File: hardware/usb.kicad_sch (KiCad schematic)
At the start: 16 parts, among them J4 USB_C_Receptacle_USB2.0_14P, J5 USB_C_Receptacle_USB2.0_14P, J6 USB_C_Receptacle_USB2.0_14P, U1 ECP5U_12_CABGA256, U10 TPD2EUSB30A, U6 FT231XQ, U8 TPD2EUSB30A, U9 TPD2EUSB30A

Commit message: Routed most of sdram
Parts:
- R15, R16, R17, R18, R19, R20: footprint Resistor_SMD:R_0603_1608Metric -> Resistor_SMD:R_0402_1005Metric
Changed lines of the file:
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@@
 			)
 		)
-		(property "Datasheet" ""
+		(property "Datasheet" "https://www.lcsc.com/datasheet/lcsc_datasheet_2411220131_Lattice-LFE5U-25F-6BG256C_C1521614.pdf"
 			(at 147.32 2.54 0)
 			(effects
@@
 			)
 		)
-		(property "Footprint" "Resistor_SMD:R_0603_1608Metric"
+		(property "Footprint" "Resistor_SMD:R_0402_1005Metric"
 			(at 54.61 155.702 90)
 			(effects
@@
 			)
 		)
-		(property "Footprint" "Resistor_SMD:R_0603_1608Metric"
+		(property "Footprint" "Resistor_SMD:R_0402_1005Metric"
 			(at 62.23 29.972 90)
 			(effects
@@
 			)
 		)
-		(property "Footprint" "Resistor_SMD:R_0603_1608Metric"
+		(property "Footprint" "Resistor_SMD:R_0402_1005Metric"
 			(at 54.61 156.718 90)
 			(effects
@@
 			)
 		)
-		(property "Footprint" "Resistor_SMD:R_0603_1608Metric"
+		(property "Footprint" "Resistor_SMD:R_0402_1005Metric"
 			(at 55.88 98.552 90)
 			(effects
@@
 			)
 		)
-		(property "Footprint" "Resistor_SMD:R_0603_1608Metric"
+		(property "Footprint" "Resistor_SMD:R_0402_1005Metric"
 			(at 55.88 99.568 90)
 			(effects
@@
 			)
 		)
-		(property "Footprint" "Resistor_SMD:R_0603_1608Metric"
+		(property "Footprint" "Resistor_SMD:R_0402_1005Metric"
 			(at 62.23 30.988 90)
 			(effects

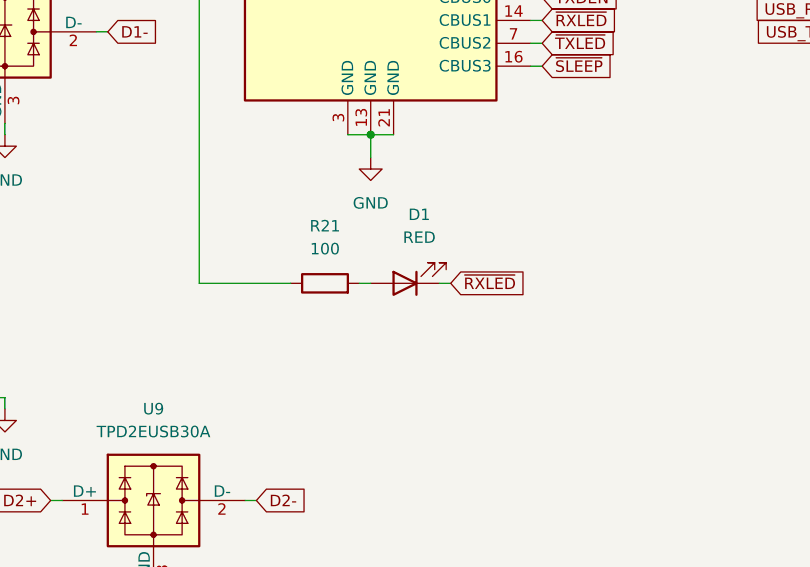
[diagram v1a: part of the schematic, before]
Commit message: Added the decoupling capacitors
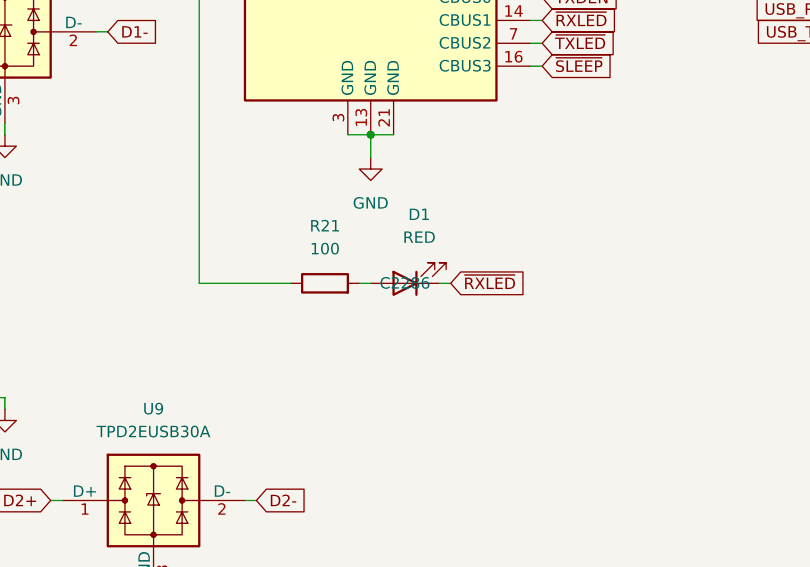
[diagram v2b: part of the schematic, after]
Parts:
- D1: JLCPCB Part # (none) -> C2286
- R15, R16, R17, R18, R19, R20: JLCPCB Part # (none) -> C25905
- R21: JLCPCB Part # (none) -> C25076
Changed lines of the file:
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@@
+			)
+		)
+		(property "JLCPCB Part #" "C25905 "
+			(at 54.61 157.48 0)
+			(effects
+				(font
+					(size 1.27 1.27)
+				)
+				(hide yes)
 			)
 		)
@@
 			)
 		)
+		(property "JLCPCB Part #" "C2286 "
+			(at 107.95 86.36 0)
+			(effects
+				(font
+					(size 1.27 1.27)
+				)
+			)
+		)
 		(pin "2"
 		)
@@
 			)
 		)
+		(property "JLCPCB Part #" "C25076 "
+			(at 99.06 86.36 0)
+			(effects
+				(font
+					(size 1.27 1.27)
+				)
+				(hide yes)
+			)
+		)
 		(pin "2"
 		)
@@
 			)
 		)
+		(property "JLCPCB Part #" "C25905 "
+			(at 62.23 31.75 0)
+			(effects
+				(font
+					(size 1.27 1.27)
+				)
+				(hide yes)
+			)
+		)
 		(pin "1"
 		)
@@
 			)
 		)
+		(property "JLCPCB Part #" "C25905 "
+			(at 54.61 154.94 0)
+			(effects
+				(font
+					(size 1.27 1.27)
+				)
+				(hide yes)
+			)
+		)
 		(pin "1"
 		)
@@
 			)
 		)
+		(property "JLCPCB Part #" "C25905 "
+			(at 55.88 100.33 0)
+			(effects
+				(font
+					(size 1.27 1.27)
+				)
+				(hide yes)
+			)
+		)
 		(pin "1"
 		)
@@
 			)
 		)
+		(property "JLCPCB Part #" "C25905 "
+			(at 55.88 97.79 0)
+			(effects
+				(font
+					(size 1.27 1.27)
+				)
+				(hide yes)
+			)
+		)
 		(pin "1"
 		)
@@
 			(at 62.23 29.21 0)
 			(effects
+				(font
+					(size 1.27 1.27)
+				)
+				(hide yes)
+			)
+		)
+		(property "JLCPCB Part #" "C25905 "
+			(at 62.23 29.21 0)
+			(effects

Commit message: V1.0 Final Revision and Readme documentation
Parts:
- added TP7, TP8: TestPoint, TestPoint:TestPoint_Pad_D2.0mm, symbol Connector:TestPoint
- renumbered D1 to D5, J4 to J3, J6 to J4, R15 to R19, R16 to R20, R19 to R22, R17 to R23, R20 to R24, R18 to R25, U1 to U3, U8 to U7, U10 to U8
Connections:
- net D1+: now also TP8.1
- net D1-: now also TP7.1
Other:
- moved on the sheet: D5, J3, J4, J5, R19, R20, R21, R22, R23, R24, R25, U3I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

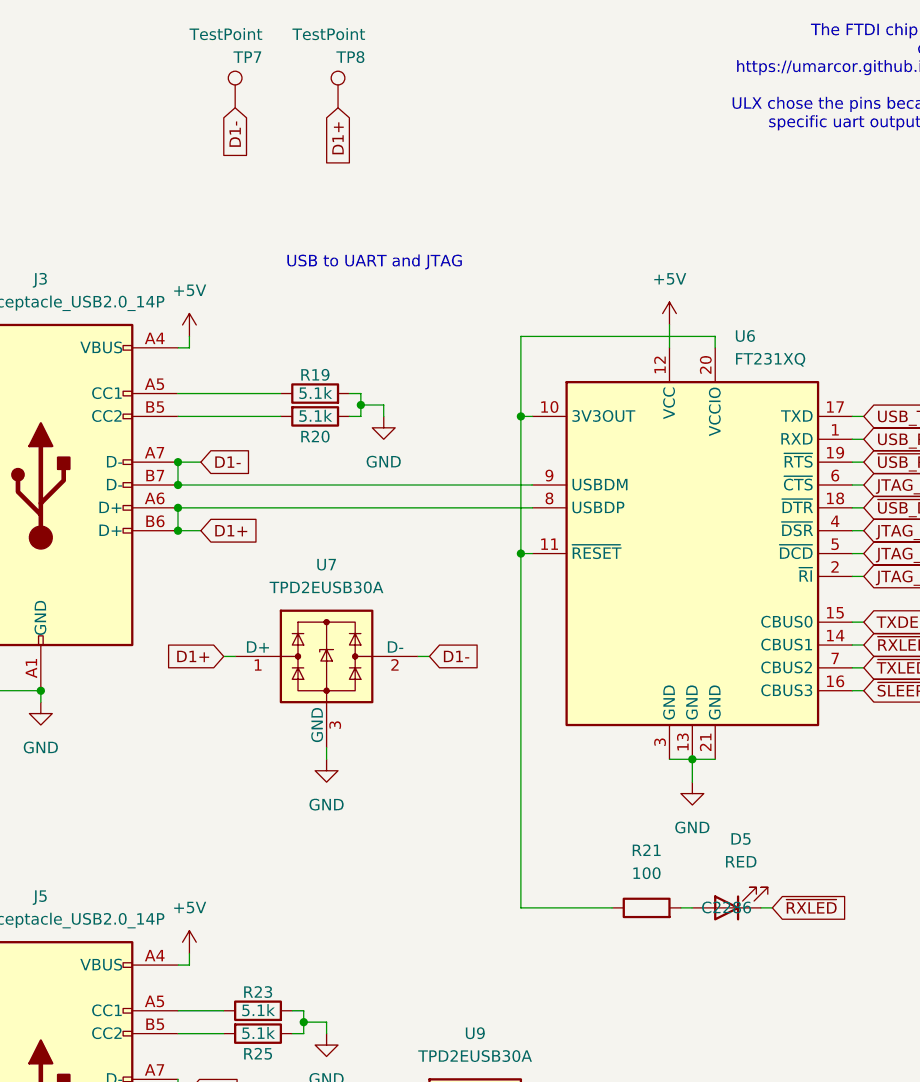
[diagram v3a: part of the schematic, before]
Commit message: Fix level shifter EN voltage error
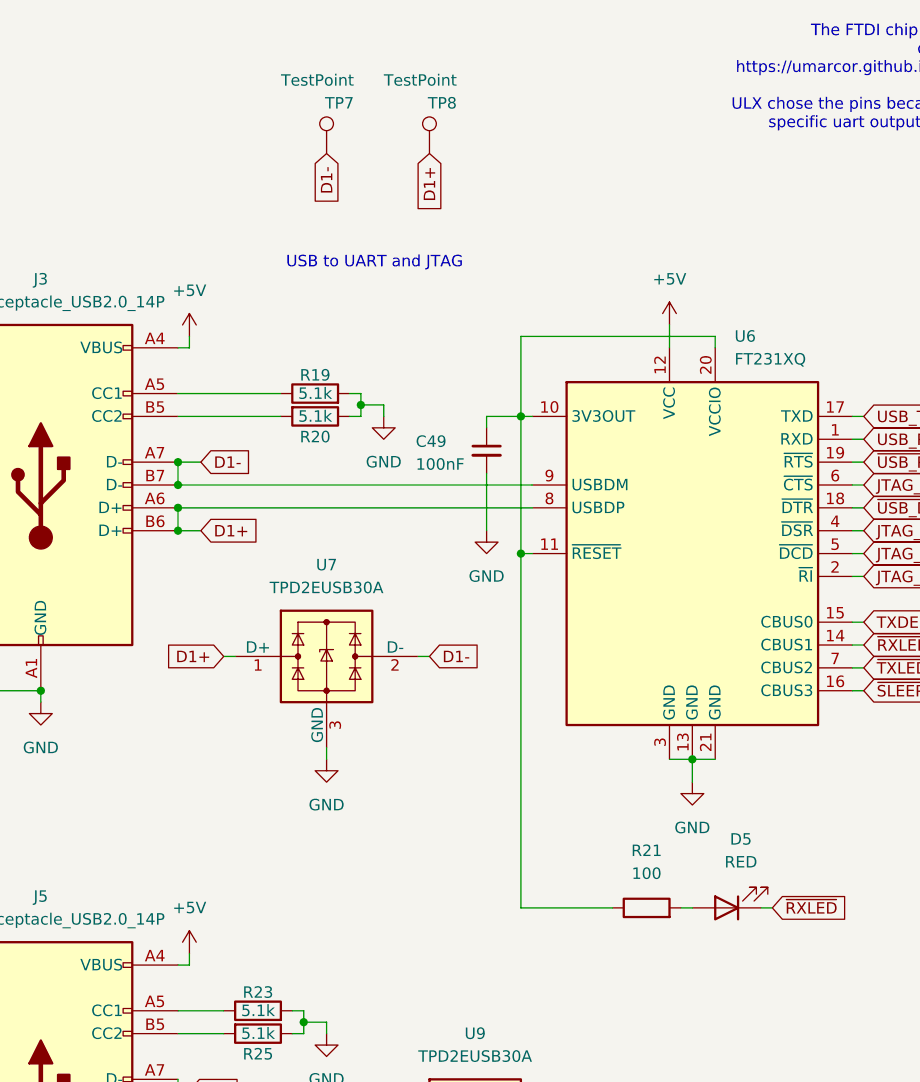
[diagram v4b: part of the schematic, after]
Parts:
- added C49: 100nF, Capacitor_SMD:C_0402_1005Metric, symbol Device:C_Small
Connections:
- net GND: now also C49.2
- net at R21.1, U6.10 (3V3OUT), U6.11 (~{RESET})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: now also C49.1
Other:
- moved on the sheet: TP7, TP8
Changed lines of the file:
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@@
 	(wire
 		(pts
+			(xy 96.52 59.69) (xy 96.52 58.42)
+		)
+		(stroke
+			(width 0)
+			(type default)
+		)
+	)
+	(wire
+		(pts
 			(xy 63.5 119.38) (xy 62.23 119.38)
 		)
@@
 	(wire
 		(pts
+			(xy 96.52 58.42) (xy 100.33 58.42)
+		)
+		(stroke
+			(width 0)
+			(type default)
+		)
+	)
+	(wire
+		(pts
 			(xy 116.84 48.26) (xy 116.84 50.8)
 		)
@@
 	(wire
 		(pts
+			(xy 96.52 64.77) (xy 96.52 71.12)
+		)
+		(stroke
+			(width 0)
+			(type default)
+		)
+	)
+	(wire
+		(pts
 			(xy 46.99 157.48) (xy 46.99 158.75)
 		)
@@
 	(global_label "D1+"
 		(shape input)
-		(at 80.01 24.13 270)
+		(at 90.17 29.21 270)
 		(fields_autoplaced yes)
 		(effects
@@
 		)
 		(property "Intersheetrefs" "${INTERSHEET_REFS}"
-			(at 80.01 31.1671 90)
+			(at 90.17 36.2471 90)
 			(effects
 				(font
@@
 	(global_label "D1-"
 		(shape input)
-		(at 68.58 24.13 270)
+		(at 78.74 29.21 270)
 		(fields_autoplaced yes)
 		(effects
@@
 		)
 		(property "Intersheetrefs" "${INTERSHEET_REFS}"
-			(at 68.58 31.1671 90)
+			(at 78.74 36.2471 90)
 			(effects
 				(font
@@
 	)
 	(symbol
+		(lib_id "Device:C_Small")
+		(at 96.52 62.23 0)
+		(unit 1)
+		(exclude_from_sim no)
+		(in_bom yes)
+		(on_board yes)
+		(dnp no)
+		(property "Reference" "C49"
+			(at 88.646 61.214 0)
+			(effects
+				(font
+					(size 1.27 1.27)
+				)
+				(justify left)
+			)
+		)
+		(property "Value" "100nF"
+			(at 88.646 63.754 0)
+			(effects
+				(font
+					(size 1.27 1.27)
+				)
+				(justify left)
+			)
+		)
+		(property "Footprint" "Capacitor_SMD:C_0402_1005Metric"
+			(at 96.52 62.23 0)
+			(effects
+				(font
+					(size 1.27 1.27)
+				)
+				(hide yes)
+			)
+		)
+		(property "Datasheet" "~"
+			(at 96.52 62.23 0)
+			(effects
+				(font
+					(size 1.27 1.27)
+				)
+				(hide yes)
+			)
+		)
+		(property "Description" "Unpolarized capacitor, small symbol"
+			(at 96.52 62.23 0)
+			(effects
+				(font
+					(size 1.27 1.27)
+				)
+				(hide yes)
+			)
+		)
+		(property "JLCPCB Part #" "C307331 "
+			(at 96.52 62.23 0)
+			(effects
+				(font
+					(size 1.27 1.27)
+				)
+				(hide yes)
+			)
+		)
+		(pin "1"
+		)
+		(pin "2"
+		)
+		(instances
+			(project "icepi-zero"
+				(path "/f88da08e-cf42-4d03-a08f-3f602fe6658d/b8c813e2-b0ac-42df-b4a2-893985a7d29c"
+					(reference "C49")
+					(unit 1)
+				)
+			)
+		)
+	)
+	(symbol
 		(lib_id "Connector:TestPoint")
-		(at 80.01 24.13 0)
+		(at 90.17 29.21 0)
 		(unit 1)
 		(exclude_from_sim no)
@@
 		(dnp no)
 		(property "Reference" "TP8"
-			(at 83.058 18.542 0)
+			(at 93.218 23.622 0)
 			(effects
 				(font
@@
 		)
 		(property "Value" "TestPoint"
-			(at 83.058 16.002 0)
+			(at 93.218 21.082 0)
 			(effects
 				(font
@@
 		)
 		(property "Footprint" "TestPoint:TestPoint_Pad_D2.0mm"
-			(at 85.09 24.13 0)
+			(at 95.25 29.21 0)
 			(effects
 				(font
@@
 		)
 		(property "Datasheet" "~"
-			(at 85.09 24.13 0)
+			(at 95.25 29.21 0)
 			(effects
 				(font
@@
 		)
 		(property "Description" "test point"
-			(at 80.01 24.13 0)
+			(at 90.17 29.21 0)
 			(effects
 				(font
@@
 	)
 	(symbol
+		(lib_id "power:GND")
+		(at 96.52 71.12 0)
+		(unit 1)
+		(exclude_from_sim no)
+		(in_bom yes)
+		(on_board yes)
+		(dnp no)
+		(fields_autoplaced yes)
+		(property "Reference" "#PWR098"
+			(at 96.52 77.47 0)
+			(effects
+				(font
+					(size 1.27 1.27)
+				)
+				(hide yes)
+			)
+		)
+		(property "Value" "GND"
+			(at 96.52 76.2 0)
+			(effects
+				(font
+					(size 1.27 1.27)
+				)
+			)
+		)
+		(property "Footprint" ""
+			(at 96.52 71.12 0)
+			(effects
+				(font
+					(size 1.27 1.27)
+				)
+				(hide yes)
+			)
+		)
+		(property "Datasheet" ""
+			(at 96.52 71.12 0)
+			(effects
+				(font
+					(size 1.27 1.27)
+				)
+				(hide yes)
+			)
+		)
+		(property "Description" "Power symbol creates a global label with name \"GND\" , ground"
+			(at 96.52 71.12 0)
+			(effects
+				(font
+					(size 1.27 1.27)
+				)
+				(hide yes)
+			)
+		)
+		(pin "1"
+		)
+		(instances
+			(project "icepi-zero"
+				(path "/f88da08e-cf42-4d03-a08f-3f602fe6658d/b8c813e2-b0ac-42df-b4a2-893985a7d29c"
+					(reference "#PWR098")
+					(unit 1)
+				)
+			)
+		)
+	)
+	(symbol
 		(lib_id "Device:LED")
 		(at 123.19 113.03 180)
@@
 					(size 1.27 1.27)
 				)
+				(hide yes)
 			)
 		)
@@
 	(symbol
 		(lib_id "Connector:TestPoint")
-		(at 68.58 24.13 0)
+		(at 78.74 29.21 0)
 		(unit 1)
 		(exclude_from_sim no)
@@
 		(dnp no)
 		(property "Reference" "TP7"
-			(at 71.628 18.542 0)
+			(at 81.788 23.622 0)
 			(effects
 				(font
@@
 		)
 		(property "Value" "TestPoint"
-			(at 71.628 16.002 0)
+			(at 81.788 21.082 0)
 			(effects
 				(font
@@
 		)
 		(property "Footprint" "TestPoint:TestPoint_Pad_D2.0mm"
-			(at 73.66 24.13 0)
+			(at 83.82 29.21 0)
 			(effects
 				(font
@@
 		)
 		(property "Datasheet" "~"
-			(at 73.66 24.13 0)
+			(at 83.82 29.21 0)
 			(effects
 				(font
@@
 		)
 		(property "Description" "test point"
-			(at 68.58 24.13 0)
+			(at 78.74 29.21 0)
 			(effects
 				(font

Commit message: Add a revision
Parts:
- TP7, TP8: now not fitted
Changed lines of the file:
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@@
 		(in_bom yes)
 		(on_board yes)
-		(dnp no)
+		(dnp yes)
 		(property "Reference" "TP8"
 			(at 93.218 23.622 0)
@@
 		(in_bom yes)
 		(on_board yes)
-		(dnp no)
+		(dnp yes)
 		(property "Reference" "TP7"
 			(at 81.788 23.622 0)

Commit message: Pre-prod fixes
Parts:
- added R35, R36, R37, R38: 4.7k, Resistor_SMD:R_0402_1005Metric, symbol Device:R
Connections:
- net GND: now also R38.2
- net JTAG_TCK: now also R35.2
- net JTAG_TDI: now also R36.2
- net JTAG_TDO: now also R37.2
- net JTAG_TMS: now also R38.1
- new net +3V3: R35.1, R36.1, R37.1
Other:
- moved on the sheet: D5, R21

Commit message: Final revision
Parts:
- C49: JLCPCB Part # C307331 -> (none); LCSC Part # (none) -> C307331
- D5: JLCPCB Part # C2286 -> (none); LCSC Part # (none) -> C2286
- J3, J4, J5: JLCPCB Part # C2765186 -> (none); LCSC Part # (none) -> C2765186
- R19, R20, R22, R23, R24, R25: JLCPCB Part # C25905 -> (none); LCSC Part # (none) -> C25905
- R21: JLCPCB Part # C25076 -> (none); LCSC Part # (none) -> C25076
- R35, R36, R37, R38: JLCPCB Part # C25900 -> (none); LCSC Part # (none) -> C25900
- U3: JLCPCB Part # C1521614 -> (none); LCSC Part # (none) -> C1521614
- U6: JLCPCB Part # C132159 -> (none); LCSC Part # (none) -> C132159
- U7, U8, U9: JLCPCB Part # C3011197 -> (none); LCSC Part # (none) -> C3011197
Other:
- moved on the sheet: R35, R36, R37, R38

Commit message: Last checks
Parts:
- added TP10, TP11, TP12, TP9: TestPoint, TestPoint:TestPoint_Pad_D1.0mm, symbol Connector:TestPoint
- renumbered C49 to C38, D5 to D6, R19 to R20, R20 to R21, R35 to R22, R36 to R23, R37 to R24, R38 to R25, R22 to R26, R24 to R27, R21 to R28, R23 to R29, R25 to R30, U3 to U1
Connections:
- net JTAG_TCK: now also TP9.1
- net JTAG_TDI: now also TP10.1
- net JTAG_TDO: now also TP11.1
- net JTAG_TMS: now also TP12.1
- net TXDEN: no longer names the net of U6.15 (CBUS0)
- net ~{SLEEP}: no longer names the net of U6.16 (CBUS3)
- net ~{TXLED}: no longer names the net of U6.7 (CBUS2)
- no-connect marks 0 -> 3
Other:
- moved on the sheet: C38, D6, J3, J4, J5, R20, R21, R22, R23, R24, R25, R26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
